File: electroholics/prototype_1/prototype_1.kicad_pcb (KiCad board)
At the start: 2 copper layers, 73 parts, among them U1 Raspberry_Pi_Pico

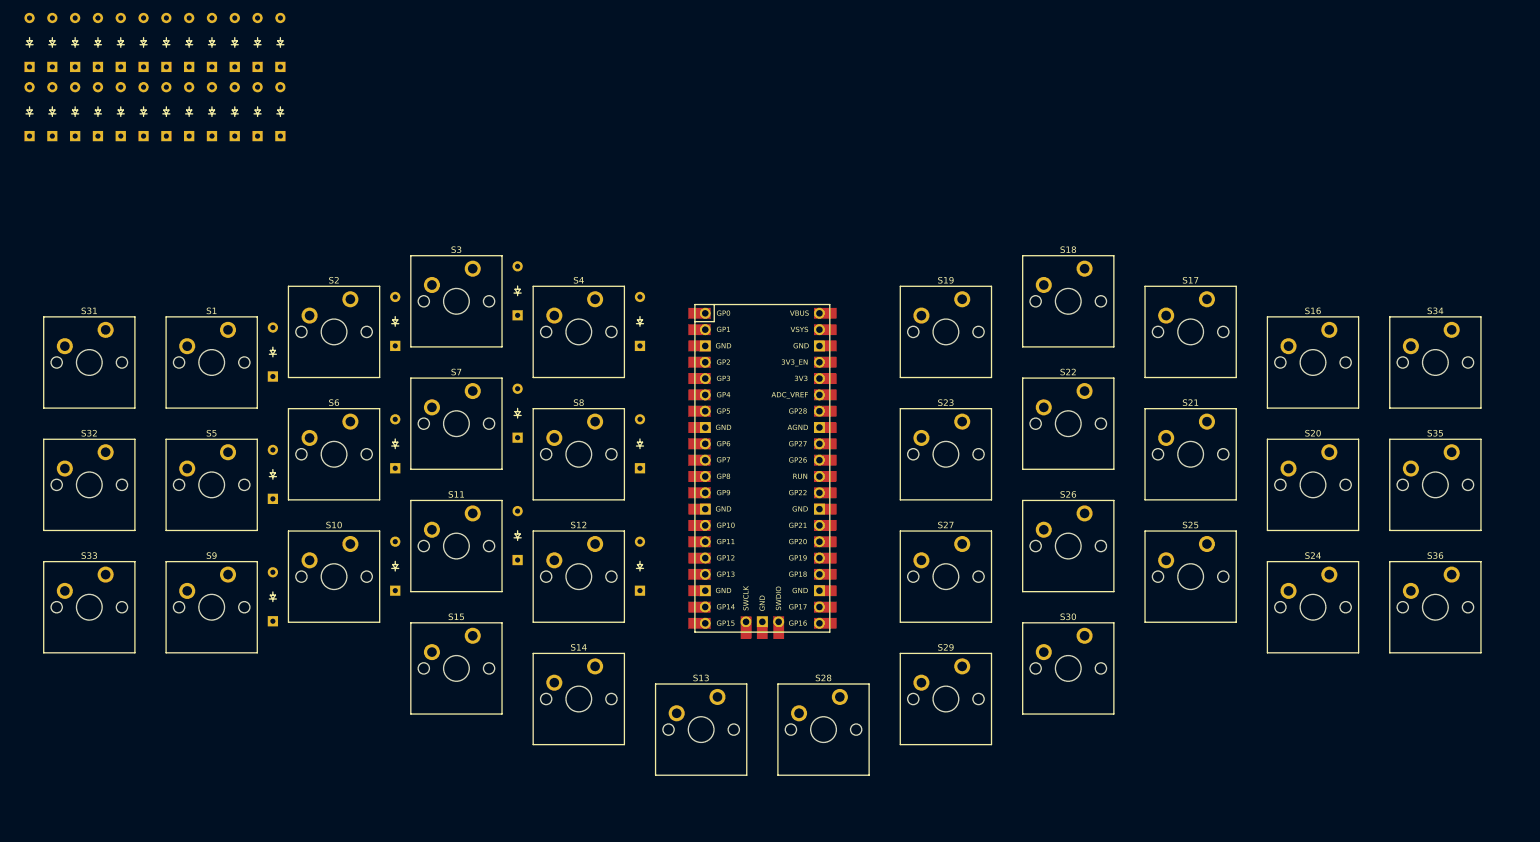
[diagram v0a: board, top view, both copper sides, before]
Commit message: removed large file
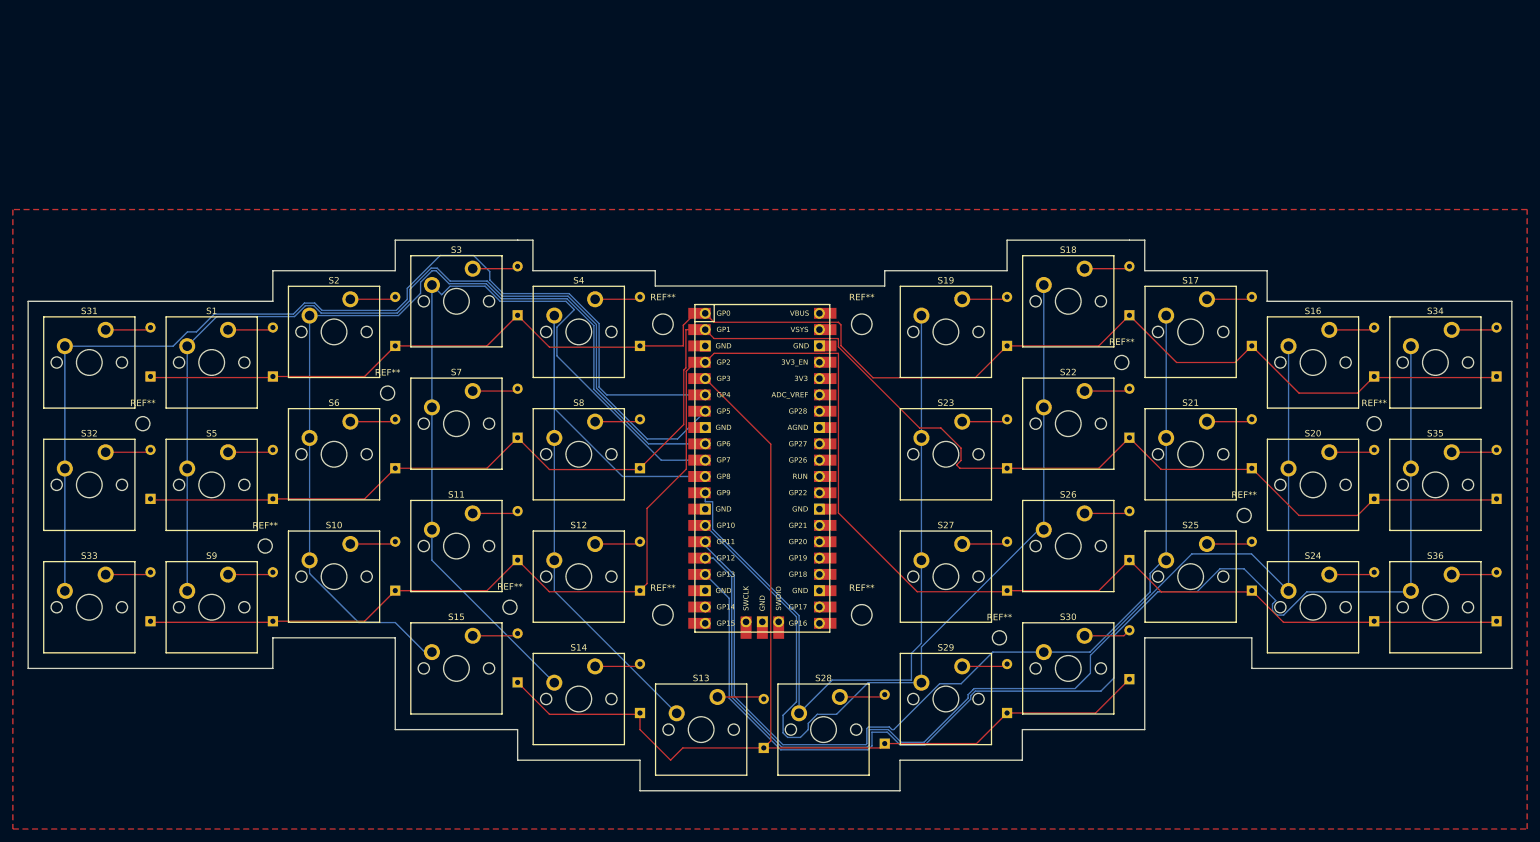
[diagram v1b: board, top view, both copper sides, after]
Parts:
- added REF**: MountingHole_2.2mm_M2, MountingHole:MountingHole_2.2mm_M2, F.Cu at (58.2, 76.5)
- added REF**: MountingHole_2.2mm_M2, MountingHole:MountingHole_2.2mm_M2, F.Cu at (210.6, 71.8)
- added REF**: MountingHole_2.2mm_M2, MountingHole:MountingHole_2.2mm_M2, F.Cu at (191.5, 47.9)
- added REF**: MountingHole_2.2mm_M2, MountingHole:MountingHole_2.2mm_M2, F.Cu at (96.3, 86.0)
- added REF**: MountingHole_2.2mm_M2, MountingHole:MountingHole_2.2mm_M2, F.Cu at (39.1, 57.5)
- added REF**: MountingHole_2.2mm_M2, MountingHole:MountingHole_2.2mm_M2, F.Cu at (172.5, 90.8)
- added REF**: MountingHole_3.2mm_M3, MountingHole:MountingHole_3.2mm_M3, F.Cu at (151.1, 42.0)
- added REF**: MountingHole_3.2mm_M3, MountingHole:MountingHole_3.2mm_M3, F.Cu at (120.1, 87.2)
- added REF**: MountingHole_2.2mm_M2, MountingHole:MountingHole_2.2mm_M2, F.Cu at (77.2, 52.7)
- added REF**: MountingHole_3.2mm_M3, MountingHole:MountingHole_3.2mm_M3, F.Cu at (151.1, 87.2)
- added REF**: MountingHole_2.2mm_M2, MountingHole:MountingHole_2.2mm_M2, F.Cu at (230.8, 57.5)
- added REF**: MountingHole_3.2mm_M3, MountingHole:MountingHole_3.2mm_M3, F.Cu at (120.1, 42.0)
- D1, D10, D11, D12, D13, D14, D15, D16, D17, D18, D19, D2, D20, D21, D22, D23, D24, D25, D26, D27, D28, D29, D3, D30, D31, D32, D33, D34, D35, D36, D4, D5, D6, D7, D8, D9: moved to B.Cu
- moved D36 208.1 mm to (249.9, 88.2)
- moved D25 207.0 mm to (211.8, 83.5)
- moved D35 204.3 mm to (249.9, 69.2)
- moved D34 202.3 mm to (249.9, 50.1)
- moved D16 202.2 mm to (230.8, 50.1)
- moved D20 192.9 mm to (230.8, 69.2)
- moved D24 186.3 mm to (230.8, 88.2)
- moved D26 184.4 mm to (192.7, 78.7)
- moved D30 180.7 mm to (192.7, 97.2)
- moved D17 179.1 mm to (211.8, 45.4)
- moved D29 170.7 mm to (173.7, 102.5)
- moved D21 169.9 mm to (211.8, 64.4)
- moved D27 166.4 mm to (173.7, 83.5)
- moved D28 161.6 mm to (154.6, 107.3)
- moved D18 156.0 mm to (192.7, 40.6)
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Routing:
- net /row2: track 0.00 -> 283.2 mm
- net /row1: track 0.00 -> 253.7 mm
- net /row0: track 0.00 -> 238.2 mm
- net /col9: track 0.00 -> 193.3 mm
- net /col8: track 0.00 -> 171.9 mm
- net /row3: track 0.00 -> 169.4 mm
- net /col0: track 0.00 -> 161.2 mm
- net /col7: track 0.00 -> 149.7 mm
- net /col2: track 0.00 -> 146.7 mm
- net /col1: track 0.00 -> 144.3 mm
- net /col6: track 0.00 -> 135.3 mm
- net /col3: track 0.00 -> 132.8 mm
- net /col5: track 0.00 -> 118.1 mm
- net /col4: track 0.00 -> 112.1 mm
- net Net-(D30-A): track 0.00 -> 7.34 mm
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- added copper zone on F.Cu, net (none)
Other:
- board outline added: 231 x 85.7 mm
